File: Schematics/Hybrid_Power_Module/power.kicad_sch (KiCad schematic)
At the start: 93 parts, among them J1 ScrewSwitch, J2 Battery, J3 ScrewSwitch, J4 GSE, Q1 AO4447A, Q2 TSM2309CX, Q3 DMN6040SSD-13, U1 TPS61175PWPR, U10 LM66100DCKR, U11 LM66100DCKR, U12 AMS1117-3.3, U2 LM74700QDBVRQ1, U3 LM74700QDBVRQ1, U4 ACS37041KLHBLT-010B3, U5 ACS37041KLHBLT-010B5, U6 INA181A2, U7 LMR51430XDDCR, U8 LMR51430XDDCR, U9 LM66100DCKR

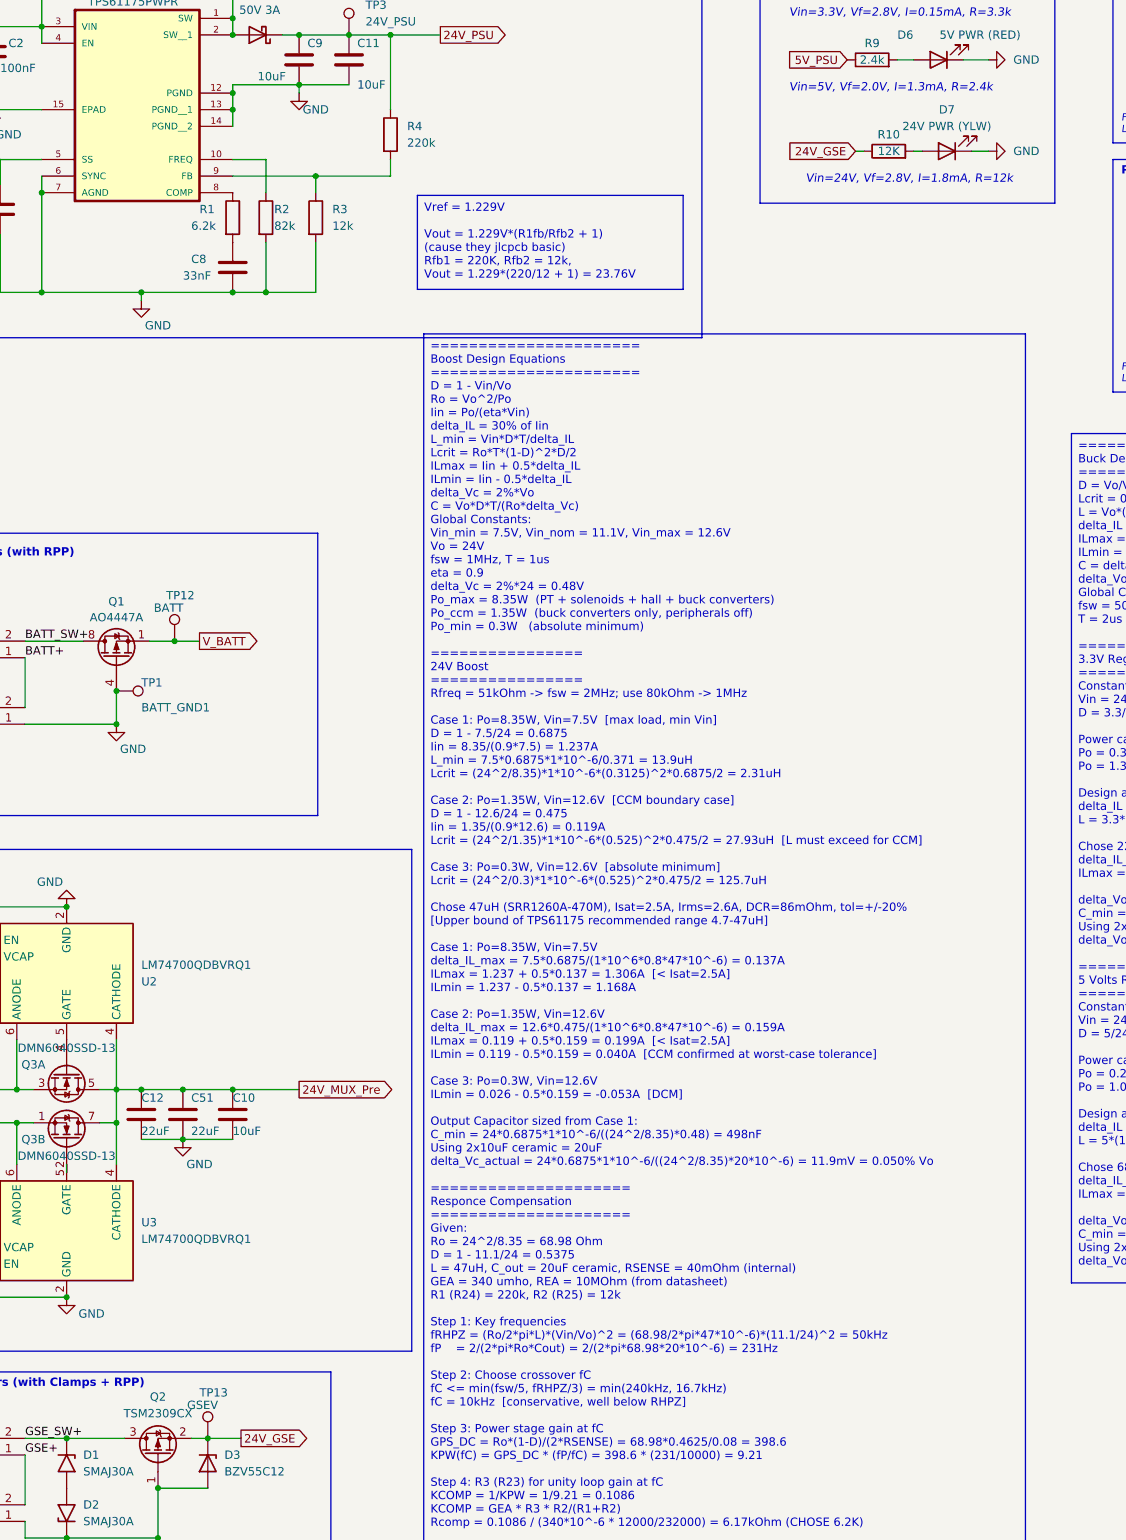
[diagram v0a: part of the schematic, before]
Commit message: fix part number and bom formation, update mostfet based on stock
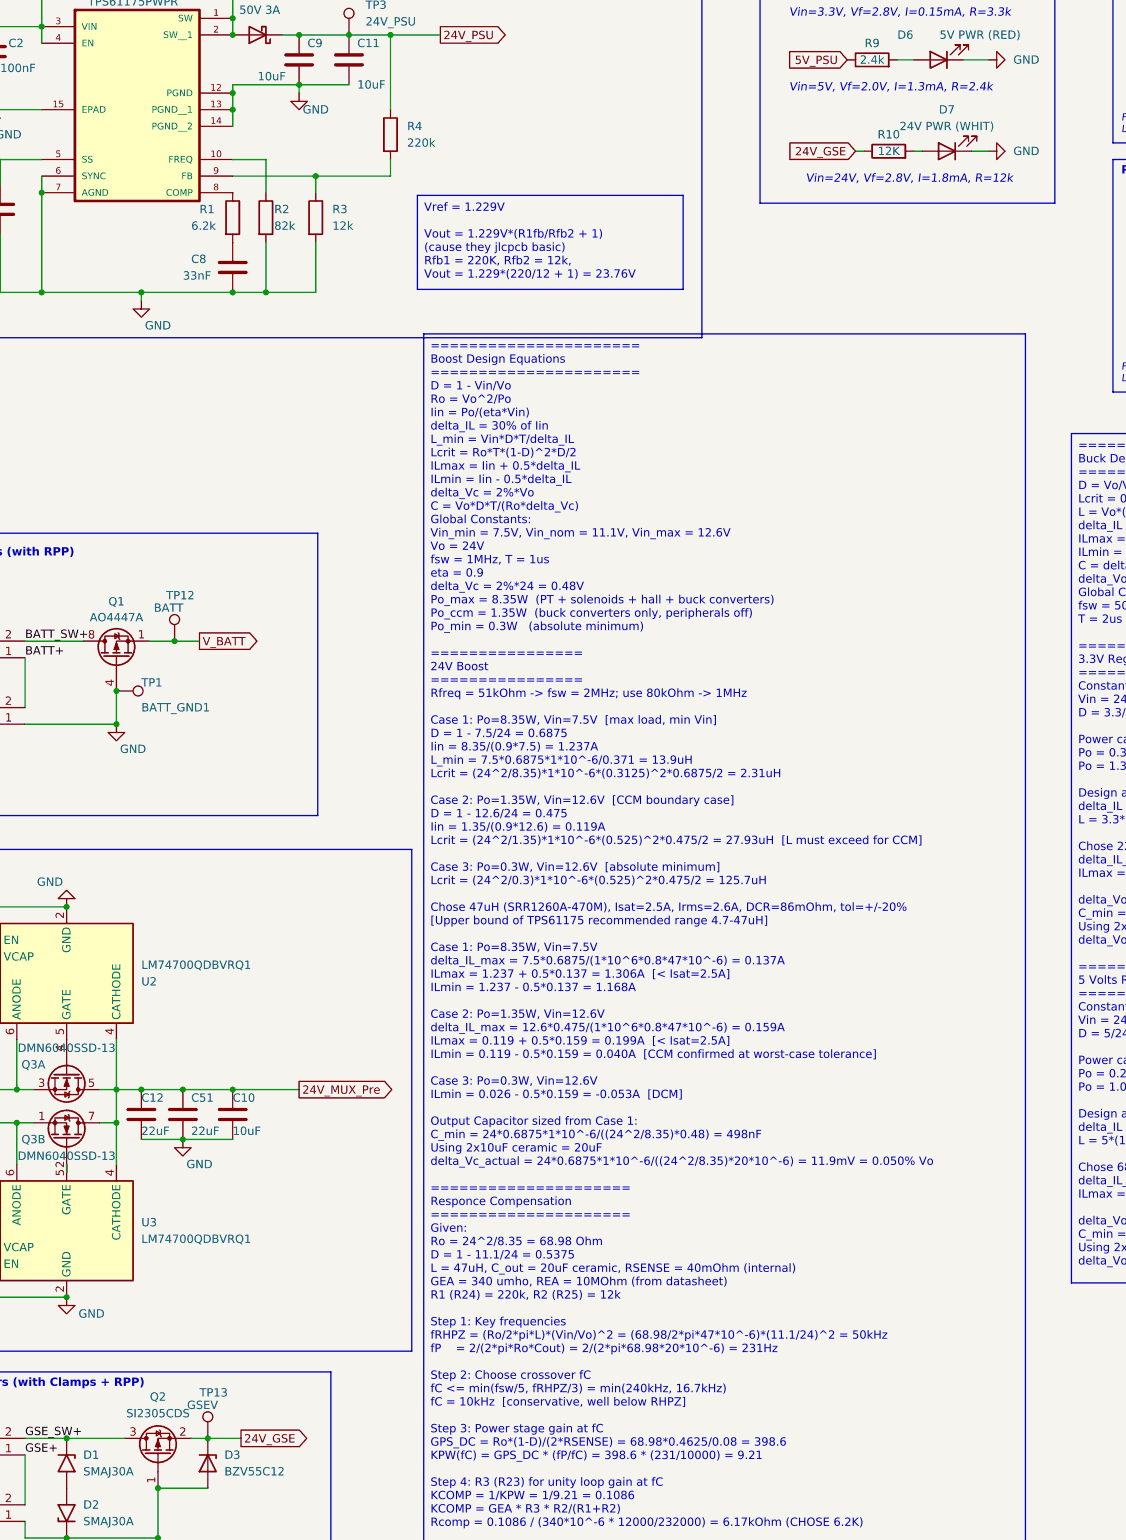
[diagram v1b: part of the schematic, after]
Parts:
- C1, C14: JLCPCB C1779 -> (none); LCSC (none) -> C1779
- C10, C11, C18, C19, C9: JLCPCB C13585 -> (none); LCSC (none) -> C13585
- C13, C15, C16, C17, C2, C20, C21, C22, C23: JLCPCB C14663 -> (none); LCSC (none) -> C14663
- C24, C25, C26, C27, C37: JLCPCB C15850 -> (none); LCSC (none) -> C15850
- C28, C29, C30, C4, C5, C6, C7: JLCPCB C15849 -> (none); LCSC (none) -> C15849
- C3: JLCPCB C57112 -> (none); LCSC (none) -> C57112
- C31, C32: JLCPCB C96446 -> (none); LCSC (none) -> C96446
- C8: JLCPCB C21117 -> (none); LCSC (none) -> C21117
- D1, D2: JLCPCB C113965 -> (none); LCSC (none) -> C113965
- D3: JLCPCB C545360 -> (none); LCSC (none) -> C545360
- D5: JLCPCB C2297 -> (none); LCSC (none) -> C2297
- D6: JLCPCB C84256 -> (none); LCSC (none) -> C84256
- D7: value 24V PWR (YLW) -> 24V PWR (WHIT); JLCPCB C34499 -> (none); LCSC (none) -> C34499
- Q1: JLCPCB C125867 -> (none); LCSC (none) -> C125867
- Q2: value TSM2309CX -> SI2305CDS; JLCPCB C2977534 -> (none); LCSC (none) -> C5182095
- Q3: JLCPCB C154876 -> (none); LCSC (none) -> C154876
- R1: JLCPCB C4260 -> (none); LCSC (none) -> C4260
- R10, R3: JLCPCB C22790 -> (none); LCSC (none) -> C22790
- R11, R5, R7: JLCPCB C22984 -> (none); LCSC (none) -> C22984
- R12: JLCPCB C21190 -> (none); LCSC (none) -> C21190
- R13, R14: JLCPCB C25804 -> (none); LCSC (none) -> C25804
- R15, R16: JLCPCB C25803 -> (none); LCSC (none) -> C25803
- R17: JLCPCB C31850 -> (none); LCSC (none) -> C31850
- R18: JLCPCB C23206 -> (none); LCSC (none) -> C23206
- R19: JLCPCB C23234 -> (none); LCSC (none) -> C23234
- R2: JLCPCB C23254 -> (none); LCSC (none) -> C23254
- R4: JLCPCB C22961 -> (none); LCSC (none) -> C22961
- R8: JLCPCB C22978 -> (none); LCSC (none) -> C22978
- R9: JLCPCB C22940 -> (none); LCSC (none) -> C22940
- U1: JLCPCB C43276 -> (none); LCSC (none) -> C43276
- U10, U11, U9: JLCPCB C2869734 -> (none); LCSC (none) -> C2869734
- U12: JLCPCB C6186 -> (none); LCSC (none) -> C6186
- U2, U3: JLCPCB C2941042 -> (none); LCSC (none) -> C2941042
- U6: JLCPCB C192764 -> (none); LCSC (none) -> C192764
- U7, U8: JLCPCB C5185863 -> (none); LCSC (none) -> C5185863

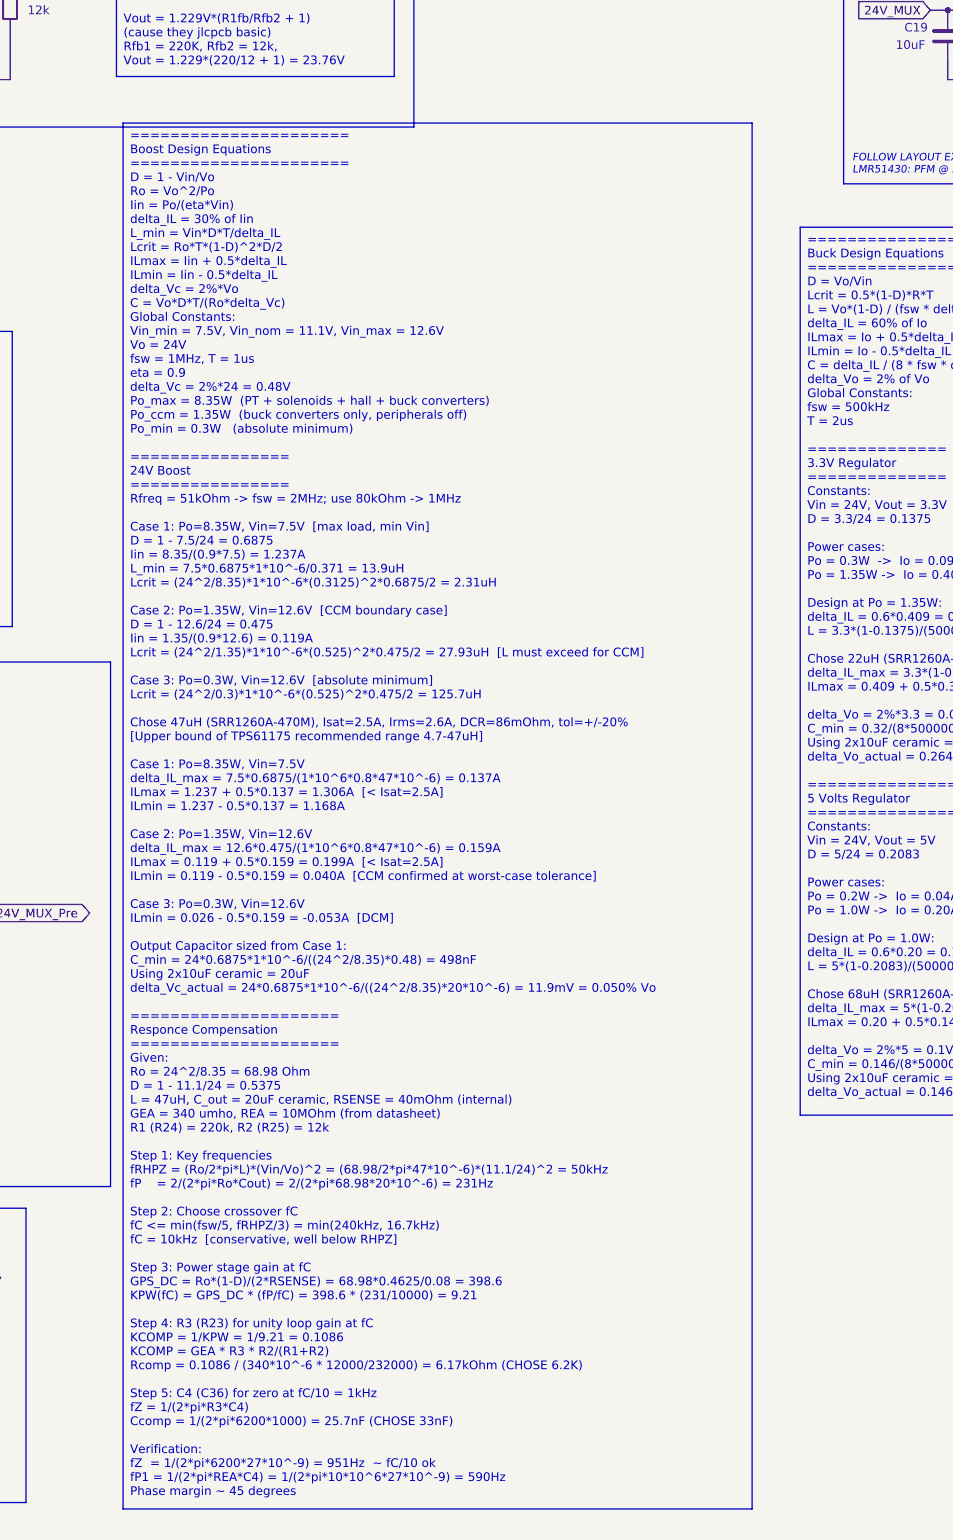
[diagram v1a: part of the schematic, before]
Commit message: finished power board silkscreen, needs final review before approval
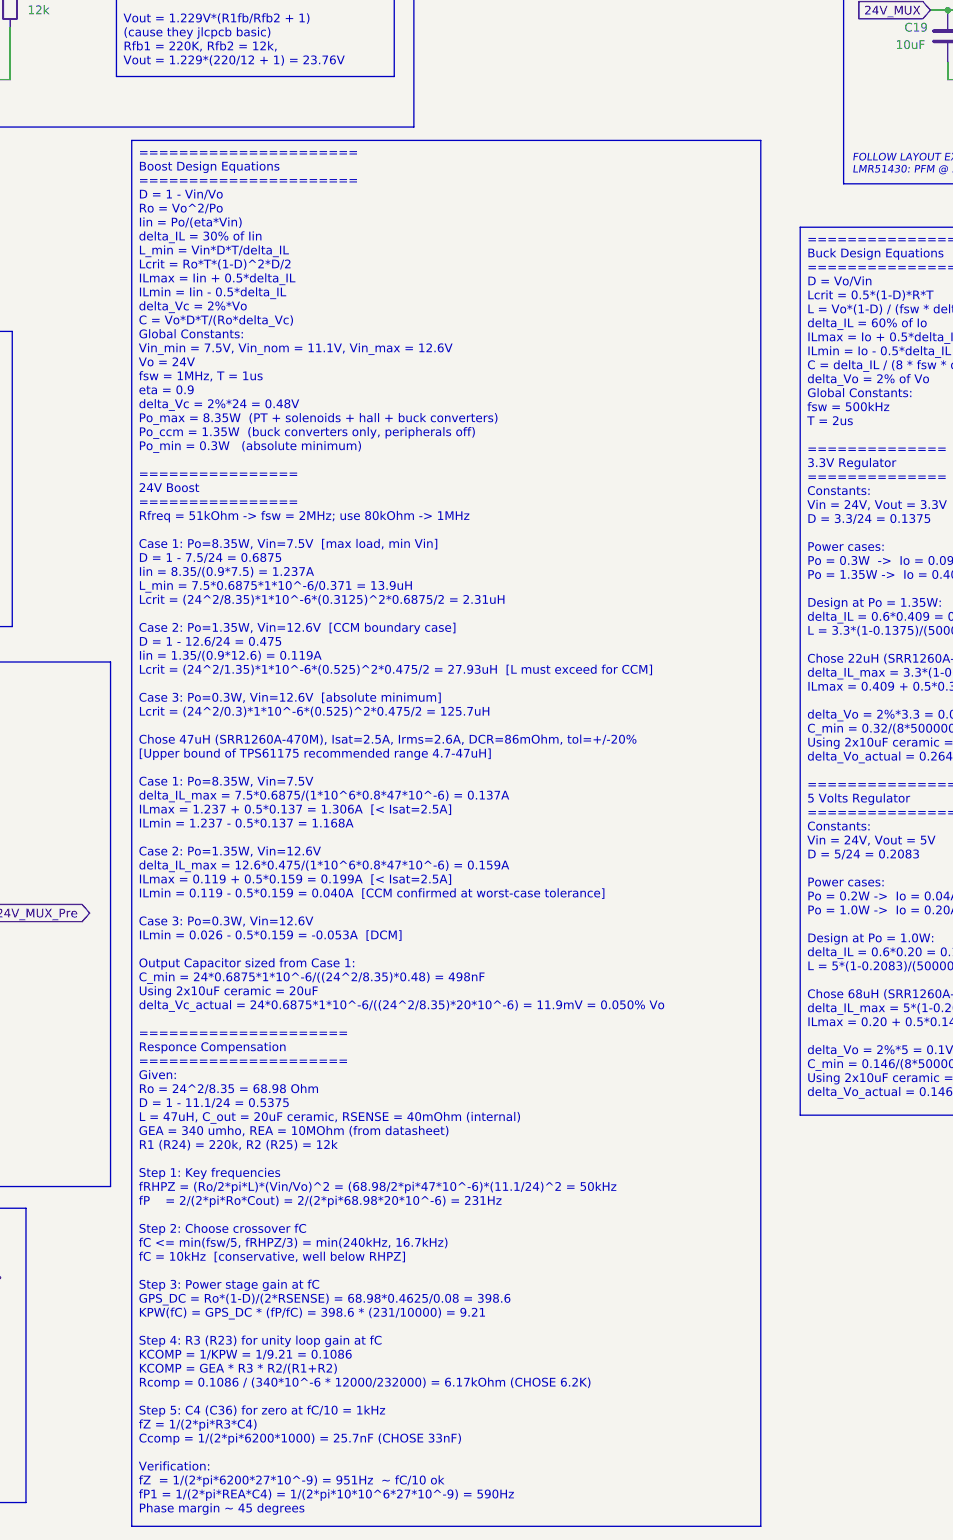
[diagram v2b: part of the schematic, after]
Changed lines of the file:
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@@
 	(text_box "======================\nBoost Design Equations\n======================\nD = 1 - Vin/Vo\nRo = Vo^2/Po\nIin = Po/(eta*Vin)\ndelta_IL = 30% of Iin\nL_min = Vin*D*T/delta_IL\nLcrit = Ro*T*(1-D)^2*D/2\nILmax = Iin + 0.5*delta_IL\nILmin = Iin - 0.5*delta_IL\ndelta_Vc = 2%*Vo\nC = Vo*D*T/(Ro*delta_Vc)\nGlobal Constants:\nVin_min = 7.5V, Vin_nom = 11.1V, Vin_max = 12.6V\nVo = 24V\nfsw = 1MHz, T = 1us\neta = 0.9\ndelta_Vc = 2%*24 = 0.48V\nPo_max = 8.35W  (PT + solenoids + hall + buck converters)\nPo_ccm = 1.35W  (buck converters only, peripherals off)\nPo_min = 0.3W   (absolute minimum)\n\n================\n24V Boost\n================\nRfreq = 51kOhm -> fsw = 2MHz; use 80kOhm -> 1MHz\n\nCase 1: Po=8.35W, Vin=7.5V  [max load, min Vin]\nD = 1 - 7.5/24 = 0.6875\nIin = 8.35/(0.9*7.5) = 1.237A\nL_min = 7.5*0.6875*1*10^-6/0.371 = 13.9uH\nLcrit = (24^2/8.35)*1*10^-6*(0.3125)^2*0.6875/2 = 2.31uH\n\nCase 2: Po=1.35W, Vin=12.6V  [CCM boundary case]\nD = 1 - 12.6/24 = 0.475\nIin = 1.35/(0.9*12.6) = 0.119A\nLcrit = (24^2/1.35)*1*10^-6*(0.525)^2*0.475/2 = 27.93uH  [L must exceed for CCM]\n\nCase 3: Po=0.3W, Vin=12.6V  [absolute minimum]\nLcrit = (24^2/0.3)*1*10^-6*(0.525)^2*0.475/2 = 125.7uH\n\nChose 47uH (SRR1260A-470M), Isat=2.5A, Irms=2.6A, DCR=86mOhm, tol=+/-20%\n[Upper bound of TPS61175 recommended range 4.7-47uH]\n\nCase 1: Po=8.35W, Vin=7.5V\ndelta_IL_max = 7.5*0.6875/(1*10^6*0.8*47*10^-6) = 0.137A\nILmax = 1.237 + 0.5*0.137 = 1.306A  [< Isat=2.5A]\nILmin = 1.237 - 0.5*0.137 = 1.168A\n\nCase 2: Po=1.35W, Vin=12.6V\ndelta_IL_max = 12.6*0.475/(1*10^6*0.8*47*10^-6) = 0.159A\nILmax = 0.119 + 0.5*0.159 = 0.199A  [< Isat=2.5A]\nILmin = 0.119 - 0.5*0.159 = 0.040A  [CCM confirmed at worst-case tolerance]\n\nCase 3: Po=0.3W, Vin=12.6V\nILmin = 0.026 - 0.5*0.159 = -0.053A  [DCM]\n\nOutput Capacitor sized from Case 1:\nC_min = 24*0.6875*1*10^-6/((24^2/8.35)*0.48) = 498nF\nUsing 2x10uF ceramic = 20uF\ndelta_Vc_actual = 24*0.6875*1*10^-6/((24^2/8.35)*20*10^-6) = 11.9mV = 0.050% Vo\n\n=====================\nResponce Compensation\n=====================\nGiven:\nRo = 24^2/8.35 = 68.98 Ohm\nD = 1 - 11.1/24 = 0.5375\nL = 47uH, C_out = 20uF ceramic, RSENSE = 40mOhm (internal)\nGEA = 340 umho, REA = 10MOhm (from datasheet)\nR1 (R24) = 220k, R2 (R25) = 12k\n\nStep 1: Key frequencies\nfRHPZ = (Ro/2*pi*L)*(Vin/Vo)^2 = (68.98/2*pi*47*10^-6)*(11.1/24)^2 = 50kHz\nfP    = 2/(2*pi*Ro*Cout) = 2/(2*pi*68.98*20*10^-6) = 231Hz\n\nStep 2: Choose crossover fC\nfC <= min(fsw/5, fRHPZ/3) = min(240kHz, 16.7kHz)\nfC = 10kHz  [conservative, well below RHPZ]\n\nStep 3: Power stage gain at fC\nGPS_DC = Ro*(1-D)/(2*RSENSE) = 68.98*0.4625/0.08 = 398.6\nKPW(fC) = GPS_DC * (fP/fC) = 398.6 * (231/10000) = 9.21\n\nStep 4: R3 (R23) for unity loop gain at fC\nKCOMP = 1/KPW = 1/9.21 = 0.1086\nKCOMP = GEA * R3 * R2/(R1+R2)\nRcomp = 0.1086 / (340*10^-6 * 12000/232000) = 6.17kOhm (CHOSE 6.2K)\n\nStep 5: C4 (C36) for zero at fC/10 = 1kHz\nfZ = 1/(2*pi*R3*C4)\nCcomp = 1/(2*pi*6200*1000) = 25.7nF (CHOSE 33nF)\n\nVerification:\nfZ  = 1/(2*pi*6200*27*10^-9) = 951Hz  ~ fC/10 ok\nfP1 = 1/(2*pi*REA*C4) = 1/(2*pi*10*10^6*27*10^-9) = 590Hz\nPhase margin ~ 45 degrees\n"
 		(exclude_from_sim no)
-		(at 105.41 78.74 0)
+		(at 106.68 81.28 0)
 		(size 92.0242 202.7428)
 		(stroke

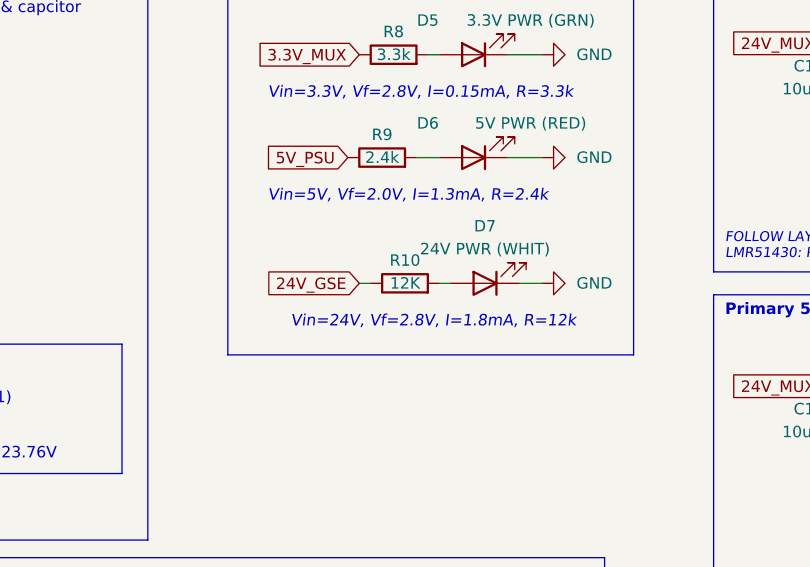
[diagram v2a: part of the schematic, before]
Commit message: minor updates to part numbers and silkscreen
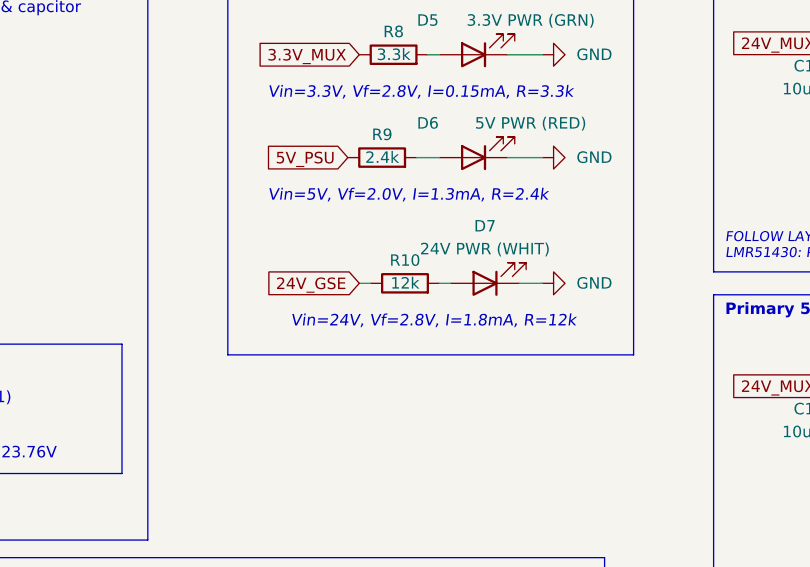
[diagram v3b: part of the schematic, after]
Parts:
- R10: value 12K -> 12k
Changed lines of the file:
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@@
 			)
 		)
-		(property "Value" "12K"
+		(property "Value" "12k"
 			(at 176.53 50.8 90)
 			(effects
